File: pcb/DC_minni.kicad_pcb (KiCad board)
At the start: 4 copper layers, 75 x 87.7 mm, 59 parts, among them J1 DRUCKSENSOR, U1 ESP32-DevKitC, U2 USB-C to DIP PCB

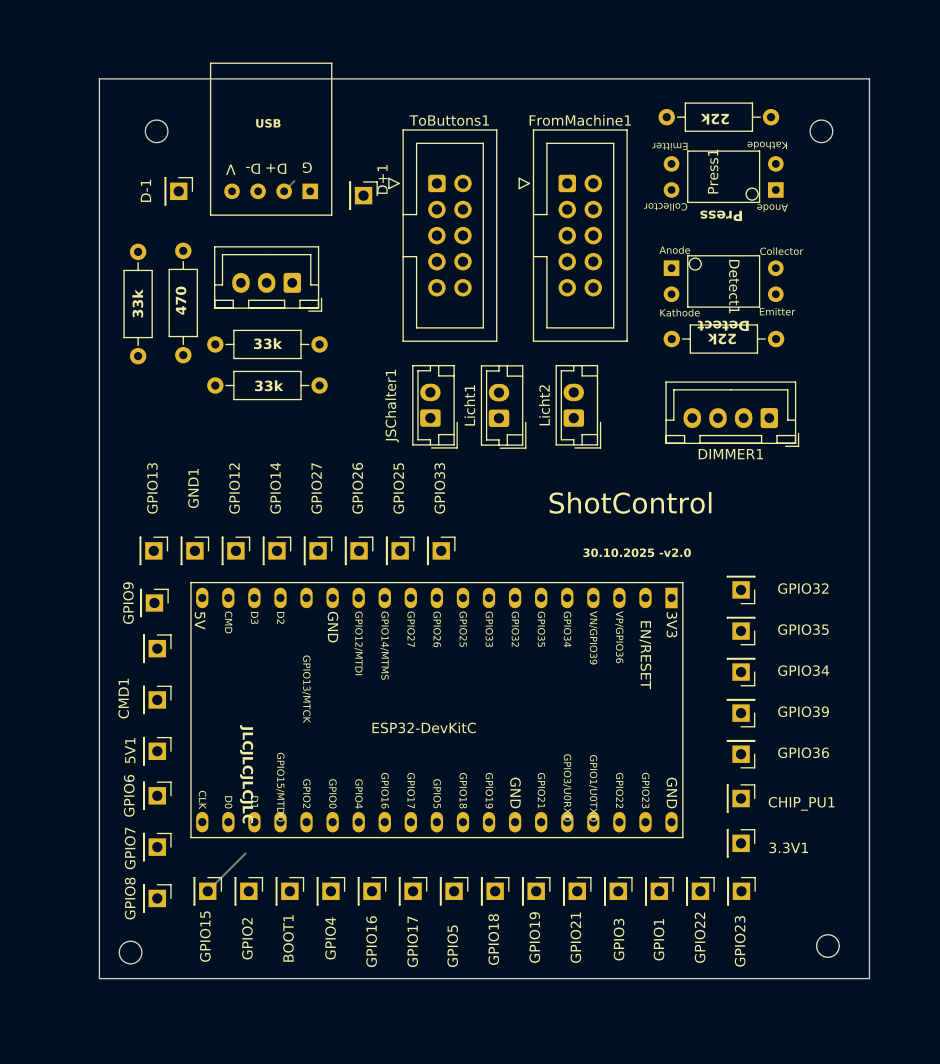
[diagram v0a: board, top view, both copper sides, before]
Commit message: Add Encoder to PCB, Update layout
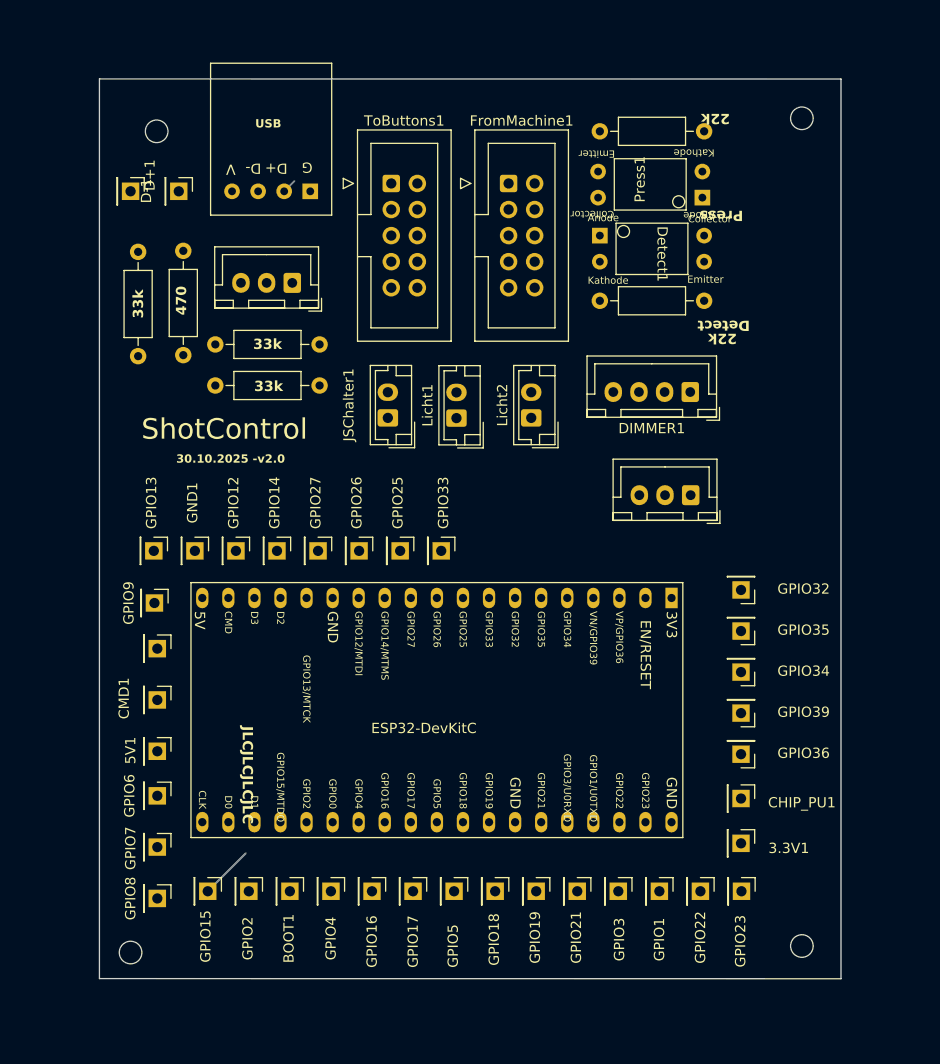
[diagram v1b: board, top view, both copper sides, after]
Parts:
- added J2: Encoder, Connector_JST:JST_XH_B3B-XH-A_1x03_P2.50mm_Vertical, F.Cu at (255.2, 115.5)
- moved D+1 22.7 mm to (200.7, 85.9)
- moved DIMMER1 8.11 mm to (255.2, 105.4)
- moved R_GND2 7.94 mm to (256.5, 96.5)
- moved Detect1 7.67 mm to (251.3, 91.5)
- moved Press1 7.19 mm to (251.5, 85.1)
- moved R_GND1 6.66 mm to (256.5, 80.0)
- moved FromMachine1 5.72 mm to (237.5, 85.1)
- moved ToButtons1 4.44 mm to (226.1, 85.1)
- moved JSChalter1 4.15 mm to (225.7, 107.9)
- moved Licht1 4.15 mm to (232.4, 108.0)
- moved Licht2 4.15 mm to (239.7, 107.9)
- moved REF** 2.54 mm to (266.1, 159.4)
- moved REF** 2.29 mm to (266.1, 78.7)
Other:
- board size 75 x 87.7 mm -> 72.2 x 87.7 mm

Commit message: PCB routing
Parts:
- removed CHIP_PU1, GPIO32: Conn_01x01_Socket, Connector_PinHeader_2.54mm:PinHeader_1x01_P2.54mm_Vertical
- moved REF** 35.0 mm to (259.1, 113.0)
- moved 3.3V1 29.6 mm to (252.2, 120.9)
- moved GPIO35 26.4 mm to (234.9, 120.9)
- moved GPIO34 24.0 mm to (239.3, 120.9)
- moved GPIO36 23.3 mm to (247.9, 120.9)
- moved GPIO39 23.1 mm to (243.3, 120.9)
- moved REF** 8.09 mm to (258.0, 158.8)
- moved GPIO8 5.41 mm to (202.9, 149.4)
- moved GPIO15 5.27 mm to (202.9, 153.4)
- moved D+1 5.20 mm to (205.3, 88.2)
- moved BOOT1 4.80 mm to (211.4, 153.7)
- moved GPIO1 4.80 mm to (247.4, 153.7)
- moved GPIO16 4.80 mm to (219.4, 153.7)
- moved GPIO17 4.80 mm to (223.4, 153.7)
- moved GPIO18 4.80 mm to (231.4, 153.7)
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- renumbered DIMMER1 to DIMMER, GPIO13 to In, GPIO22 to OUT
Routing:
- net IN: track 0.00 -> 95.6 mm, vias 0 -> 5
- net OUT: track 0.00 -> 83.5 mm, vias 0 -> 1
- net +5V: track 0.00 -> 78.3 mm, vias 0 -> 3
- net ZeroCross: track 0.00 -> 77.0 mm, vias 0 -> 3
- net PWM: track 0.00 -> 69.2 mm, vias 0 -> 3
- net Drucksensor: track 0.40 -> 59.4 mm, vias 0 -> 1
- net +3.3V: track 0.71 -> 44.9 mm, vias 0 -> 3
- net Net-(GPIO23-Pin_1): track 0.00 -> 42.0 mm
- net Net-(GPIO25-Pin_1): track 0.00 -> 38.9 mm, vias 0 -> 3
- net Net-(JSChalter1-Pin_2): track 0.00 -> 35.0 mm, vias 0 -> 4
- net Net-(Detect1-Cathode): track 0.00 -> 22.9 mm
- net Net-(FromMachine1-Pin_1): track 0.00 -> 21.9 mm
- net Net-(RSP_01_1-Pad2): track 0.00 -> 16.2 mm, vias 0 -> 2
- net Net-(GPIO2-Pin_1): track 0.00 -> 14.9 mm, vias 0 -> 1
- net Net-(CMD1-Pin_1): track 0.00 -> 14.8 mm, vias 0 -> 1
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- added copper zone on B.Cu, net GND
- added copper zone on F.Cu, net GND
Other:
- board size 72.2 x 87.7 mm -> 64 x 85.8 mm
- board text added: "11.11.2025 -v2.0"
- board text removed: "30.10.2025 -v2.0"
- board text removed: "GPIO13/MTCK"

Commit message: Finished PCB routing
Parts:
- removed REF** (x4): MountingHole_2.2mm_M2, MountingHole:MountingHole_2.2mm_M2
- U2: value USB-C to DIP PCB -> USB-C
- moved U2 3.05 mm to (214.4, 77.7)
- renumbered Detect1 to Detect
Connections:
- U1 pad 2: Net-(CHIP_PU1-Pin_1) -> unconnected-(U1-CHIP_PU-Pad2)
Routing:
- net Net-(JSChalter1-Pin_2): track 35.0 -> 38.1 mm
- net Net-(D+1-Pin_1): track 11.3 -> 14.4 mm, vias 0 -> 1
- net Net-(D-1-Pin_1): vias 0 -> 1
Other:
- board text removed: "22k"
- board text removed: "D-"
- board text removed: "Detect"
- board text removed: "G"
- board text removed: "JLCJLCJLCJLC"
- board text removed: "USB"
- board text removed: "V"

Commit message: Implement comments from Review
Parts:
- moved RSP_3 9.18 mm to (200.5, 111.1)
- moved RSP_2 9.18 mm to (204.9, 100.8)
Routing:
- net Net-(RSP_01_1-Pad2): track 16.2 -> 8.01 mm, vias 2 -> 0
- net Drucksensor: track 59.4 -> 51.6 mm
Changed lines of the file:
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@@
 	(footprint "Resistor_THT:R_Axial_DIN0207_L6.3mm_D2.5mm_P10.16mm_Horizontal"
 		(layer "F.Cu")
-		(at 205.795 91.655 -90)
+		(at 204.940001 100.800001 -90)
 		(descr "Resistor, Axial_DIN0207 series, Axial, Horizontal, pin pitch=10.16mm, 0.25W = 1/4W, length*diameter=6.3*2.5mm^2, http://cdn-reichelt.de/documents/datenblatt/B400/1_4W%23YAG.pdf")
 		(tags "Resistor Axial_DIN0207 series Axial Horizontal pin pitch 10.16mm 0.25W = 1/4W length 6.3mm diameter 2.5mm")
@@
 	(footprint "Resistor_THT:R_Axial_DIN0207_L6.3mm_D2.5mm_P10.16mm_Horizontal"
 		(layer "F.Cu")
-		(at 201.395 101.915 90)
+		(at 200.540001 111.060001 90)
 		(descr "Resistor, Axial_DIN0207 series, Axial, Horizontal, pin pitch=10.16mm, 0.25W = 1/4W, length*diameter=6.3*2.5mm^2, http://cdn-reichelt.de/documents/datenblatt/B400/1_4W%23YAG.pdf")
 		(tags "Resistor Axial_DIN0207 series Axial Horizontal pin pitch 10.16mm 0.25W = 1/4W length 6.3mm diameter 2.5mm")
@@
 	)
 	(gr_text "470"
-		(at 206.195 97.935 90)
+		(at 205.340001 107.080001 90)
 		(layer "F.SilkS")
 		(effects
@@
 	)
 	(gr_text "33k"
-		(at 201.995 98.235 90)
+		(at 201.140001 107.380001 90)
 		(layer "F.SilkS")
 		(effects
@@
 	)
 	(segment
-		(start 208.9 98.1)
-		(end 208.9 100.76)
-		(width 0.4)
-		(layer "F.Cu")
-		(net 48)
-	)
-	(segment
-		(start 205.795 91.655)
-		(end 205.795 97.995)
-		(width 0.4)
-		(layer "F.Cu")
-		(net 48)
-	)
-	(segment
-		(start 205.795 97.995)
-		(end 205.9 98.1)
+		(start 204.940001 100.800001)
+		(end 208.889999 100.800001)
 		(width 0.4)
 		(layer "F.Cu")
@@
 		(net 48)
 	)
-	(via
-		(at 205.9 98.1)
-		(size 0.6)
-		(drill 0.3)
-		(layers "F.Cu" "B.Cu")
-		(net 48)
-	)
-	(via
-		(at 208.9 98.1)
-		(size 0.6)
-		(drill 0.3)
-		(layers "F.Cu" "B.Cu")
-		(net 48)
-	)
 	(segment
-		(start 205.9 98.1)
-		(end 208.9 98.1)
+		(start 208.889999 100.800001)
+		(end 208.915 100.775)
 		(width 0.4)
-		(layer "B.Cu")
+		(layer "F.Cu")
 		(net 48)
 	)
@@
 	)
 	(segment
-		(start 236.6 102.8)
+		(start 236.6 111)
 		(end 236.6 118.5)
 		(width 0.4)
@@
 	)
 	(via
-		(at 236.6 102.8)
+		(at 236.6 111)
 		(size 0.6)
 		(drill 0.3)
@@
 	)
 	(segment
-		(start 205.695 101.915)
-		(end 205.795 101.815)
+		(start 236.560001 110.960001)
+		(end 236.6 111)
 		(width 0.4)
 		(layer "B.Cu")
@@
 	)
 	(segment
-		(start 201.675 101.815)
-		(end 201.395 101.535)
-		(width 0.2)
-		(layer "B.Cu")
-		(net 49)
-	)
-	(segment
-		(start 205.795 101.815)
-		(end 206.594999 102.614999)
+		(start 204.940001 110.960001)
+		(end 236.560001 110.960001)
 		(width 0.4)
 		(layer "B.Cu")
@@
 	)
 	(segment
-		(start 201.395 101.915)
-		(end 205.695 101.915)
+		(start 204.840001 111.060001)
+		(end 204.940001 110.960001)
 		(width 0.4)
 		(layer "B.Cu")
@@
 	)
 	(segment
-		(start 206.594999 102.614999)
-		(end 236.414999 102.614999)
-		(width 0.4)
+		(start 200.820001 110.960001)
+		(end 200.540001 110.680001)
+		(width 0.2)
 		(layer "B.Cu")
 		(net 49)
 	)
 	(segment
-		(start 236.414999 102.614999)
-		(end 236.6 102.8)
+		(start 200.540001 111.060001)
+		(end 204.840001 111.060001)
 		(width 0.4)
 		(layer "B.Cu")
